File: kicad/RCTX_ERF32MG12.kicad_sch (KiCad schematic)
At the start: 93 parts, among them J21 USB_OTG, P1 SD Card, P2 Nokia 5110 display, P5 LEDs, Q1 Q_PMOS_DGS, SW1 RESET, U1 PIC16(L)F1459-I_ML

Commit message: Optimizing power lines
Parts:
- removed D? (x4): 1N4148, Diodes_THT:D_5W_P5.08mm_Vertical_KathodeUp, symbol RCTX-rescue:D-device
- removed HEX_SW?: RF_BAND_SEL, Buttons_Switches_THT:Nidec_Copal_SH-7010C, symbol RCTX-rescue:SW_Coded-switches
- removed J?: SWITCHES, symbol conn:Conn_02x14_Odd_Even
- added P?: SWITCHES, symbol Connector_Generic:Conn_02x15_Odd_Even
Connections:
- net +3V3: now also P?.1 (Pin_1)
- net +5V: now also P5.1 (Pin_1)
- net DSC_MODE: now also P?.25 (Pin_25)
- net GND: now also P?.10 (Pin_10), P?.12 (Pin_12), P?.14 (Pin_14), P?.16 (Pin_16), P?.18 (Pin_18), P?.2 (Pin_2), P?.20 (Pin_20), P?.22 (Pin_22), P?.24 (Pin_24), P?.26 (Pin_26), P?.28 (Pin_28), P?.4 (Pin_4), P?.6 (Pin_6), P?.8 (Pin_8)
- net RF_MODE: now also P?.29 (Pin_29)
- net SW_DATA_A: now also P?.17 (Pin_17)
- net SW_DATA_B: now also P?.15 (Pin_15)
- net SW_DATA_C: now also P?.13 (Pin_13)
- net SW_DATA_D: now also P?.11 (Pin_11)
- net SW_RF_BAND_SCAN: now also P?.3 (Pin_3)
- net SW_RX_ID_SCAN: now also P?.5 (Pin_5)
- net SW_RX_SUB_ID_SCAN: now also P?.7 (Pin_7)
- net SW_SELECTOR_SCAN: now also P?.9 (Pin_9)
- net TBD_L_1_MODE: now also P?.19 (Pin_19)
- net TBD_L_2_MODE: now also P?.21 (Pin_21)
- net TBD_L_3_MODE: now also P?.23 (Pin_23)
- net TBD_R_1_MODE: now also P?.27 (Pin_27)
- net USB_RX: now also U1.7 (TX); no longer U1.9 (RX)
- net USB_TX: now also U1.9 (RX); no longer U1.7 (TX)
- net SCK renamed SCLK
- net SDI renamed MISO
- net MISO: now also P1.3 (Pin_3); no longer P1.5 (Pin_5)
- net SDO renamed MOSI
- net MOSI: now also P1.5 (Pin_5); no longer P1.3 (Pin_3)
- net VBATT renamed +BATT
- net +BATT: no longer P5.1 (Pin_1)
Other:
- removed sheet DisplayI2C
- note added: "- UART bridge for SD card, Nokia 5110 LCD and LEDs - USB Adapter for: CMSIS-DAP/TTY/MSD (SD Card)"
- note added: "/CS"
- note added: "MISO"
- note added: "MOSI"
- note added: "SCLK"
- note added: "VLED"
- note removed: "- UART bridge for SD card and Nokia 5110 LCD - USB Adapter for: CMSIS-DAP/TTY/MSD (SD Card)"
- note removed: "SCK"
- note removed: "SD SS/CS"
- note removed: "SDI"
- note removed: "SDO"
- note removed: "VBATT"
- moved on the sheet: C1, C2, C?, D1, J21, P1, P2, P5, Q1, R1, SW1, U1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

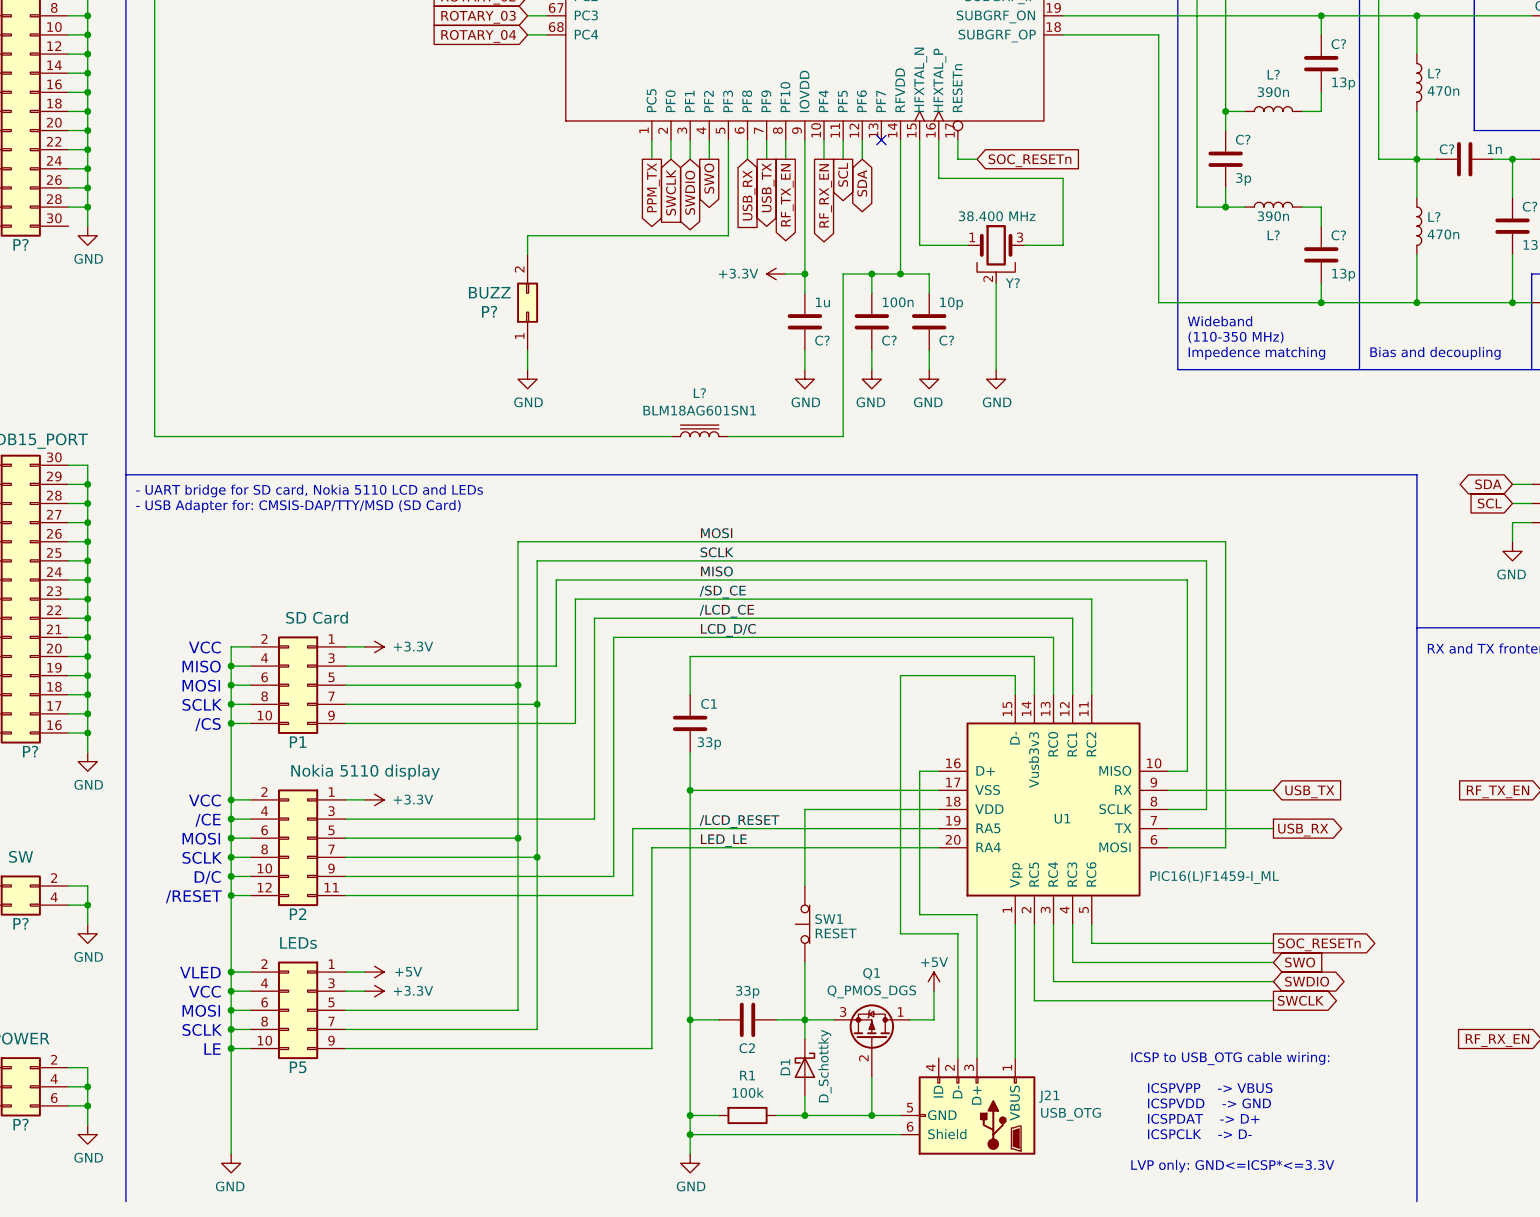
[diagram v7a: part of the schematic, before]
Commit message: Using SAMD11D14M instead of PIC16F1459 for USB bridge - updating schematics
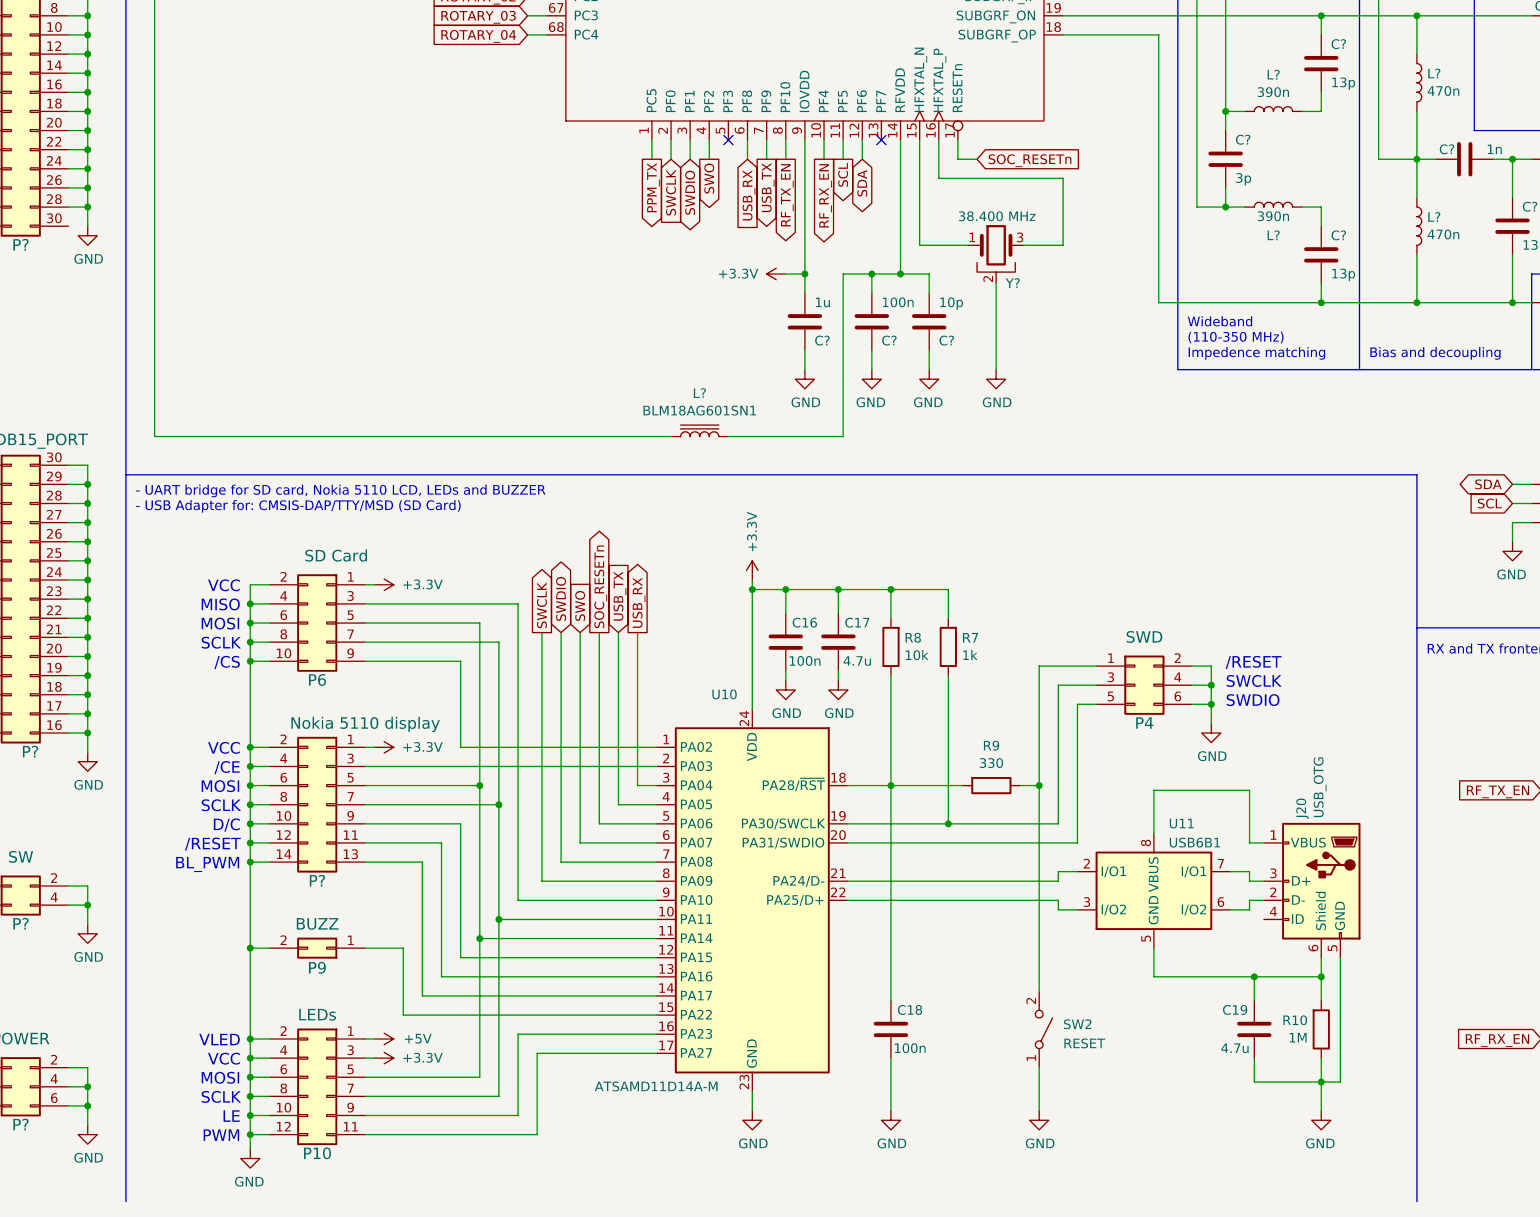
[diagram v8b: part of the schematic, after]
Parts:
- removed C1, C2: 33p, symbol device:C
- removed D1: D_Schottky, symbol device:D_Schottky
- removed J21: USB_OTG, symbol conn:USB_OTG
- removed P1: SD Card, symbol conn:Conn_02x05_Odd_Even
- removed P2: Nokia 5110 display, symbol conn:Conn_02x06_Odd_Even
- removed P5: LEDs, symbol conn:Conn_02x05_Odd_Even
- removed P?: BUZZ, symbol conn:Conn_02x01
- removed Q1: Q_PMOS_DGS, symbol device:Q_PMOS_DGS
- removed R1: 100k, symbol device:R
- removed SW1: RESET, symbol switches:SW_Push_Open
- removed U1: PIC16(L)F1459-I_ML, symbol PIC_USB_BRIDGE:PIC16(L)F1459-I_ML
- added C16, C18: 100n, symbol device:C
- added C17, C19: 4.7u, symbol device:C
- added J20: USB_OTG, symbol conn:USB_OTG
- added P10: LEDs, symbol conn:Conn_02x06_Odd_Even
- added P4: SWD, symbol conn:Conn_02x03_Odd_Even
- added P6: SD Card, symbol conn:Conn_02x05_Odd_Even
- added P9: BUZZ, symbol conn:Conn_02x01
- added P?: Nokia 5110 display, symbol Connector_Generic:Conn_02x07_Odd_Even
- added R10: 1M, symbol device:R
- added R7: 1k, symbol device:R
- added R8: 10k, symbol device:R
- added R9: 330, symbol device:R
- added SW2: RESET, symbol RCTX-rescue:SW_SPST-switches
- added U10: ATSAMD11D14A-M, Package_DFN_QFN:QFN-24-1EP_4x4mm_P0.5mm_EP2.6x2.6mm, symbol MCU_Microchip_SAMD:ATSAMD11D14A-M
- added U11: USB6B1, Package_SO:SOIC-8_3.9x4.9mm_P1.27mm, symbol Power_Protection:USB6B1
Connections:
- net +3V3: now also C16.2, C17.2, P10.3 (Pin_3), P6.1 (Pin_1), P?.1 (Pin_1), R7.2, R8.2, U10.24 (VDD)
- net +5V: now also P10.1 (Pin_1)
- net GND: now also C16.1, C17.1, C18.1, C19.1, J20.5 (GND), P10.10 (Pin_10), P10.12 (Pin_12), P10.2 (Pin_2), P10.4 (Pin_4), P10.6 (Pin_6), P10.8 (Pin_8), P4.2 (Pin_2), P4.4 (Pin_4), P4.6 (Pin_6), P6.10 (Pin_10), P6.2 (Pin_2), P6.4 (Pin_4), P6.6 (Pin_6), P6.8 (Pin_8), P9.2 (Pin_2), P?.10 (Pin_10), P?.12 (Pin_12), P?.14 (Pin_14), P?.2 (Pin_2), P?.4 (Pin_4), P?.6 (Pin_6), P?.8 (Pin_8), R10.1, SW2.1 (A), U10.23 (GND)
- net SOC_RESETn: now also U10.5 (PA06)
- net SWCLK: now also U10.8 (PA09)
- net SWDIO: now also U10.7 (PA08)
- net SWO: now also U10.6 (PA07)
- net USB_RX: now also U10.3 (PA04)
- net USB_TX: now also U10.4 (PA05)
- new net: J20.1 (VBUS), U11.1 (VBUS), U11.8 (VBUS)
- new net: U10.21 (PA24/D-), U11.2 (I/O1)
- new net: U10.22 (PA25/D+), U11.3 (I/O2)
- new net: C19.2, J20.6 (Shield), R10.2, U11.4 (GND), U11.5 (GND)
- new net: J20.2 (D-), U11.6 (I/O2)
- new net: J20.3 (D+), U11.7 (I/O1)
- new net: P4.3 (Pin_3), R7.1, U10.19 (PA30/SWCLK)
- new net: P4.1 (Pin_1), R9.1, SW2.2 (B)
- new net: P4.5 (Pin_5), U10.20 (PA31/SWDIO)
- new net: C18.2, R8.1, R9.2, U10.18 (PA28/~{RST})
- new net: P10.11 (Pin_11), U10.17 (PA27)
- new net: P10.5 (Pin_5), P6.5 (Pin_5), P?.5 (Pin_5), U10.11 (PA14)
- new net: P10.7 (Pin_7), P6.7 (Pin_7), P?.7 (Pin_7), U10.10 (PA11)
- new net: P10.9 (Pin_9), U10.16 (PA23)
- new net: P6.9 (Pin_9), U10.1 (PA02)
- new net: P?.9 (Pin_9), U10.12 (PA15)
- new net: P?.11 (Pin_11), U10.13 (PA16)
- new net: P?.13 (Pin_13), U10.14 (PA17)
- new net: P9.1 (Pin_1), U10.15 (PA22)
- new net: P?.3 (Pin_3), U10.2 (PA03)
- new net: P6.3 (Pin_3), U10.9 (PA10)
- no-connect marks 2 -> 3
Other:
- note added: "- UART bridge for SD card, Nokia 5110 LCD, LEDs and BUZZER - USB Adapter for: CMSIS-DAP/TTY/MSD (SD Card)"
- note added: "BL_PWM"
- note added: "PWM"
- note added: "SWCLK"
- note added: "SWDIO"
- note removed: "- UART bridge for SD card, Nokia 5110 LCD and LEDs - USB Adapter for: CMSIS-DAP/TTY/MSD (SD Card)"
- note removed: "ICSP to USB_OTG cable wiring: ICSPVPP -> VBUS ICSPVDD -> GND ICSPDAT -> D+ ICSPCLK -> D- LVP only: GND<=ICSP*<=3.3V"
